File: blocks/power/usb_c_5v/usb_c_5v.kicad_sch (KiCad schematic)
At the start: 3 parts, among them J1 USB Type-C Receptacle 16-pin 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

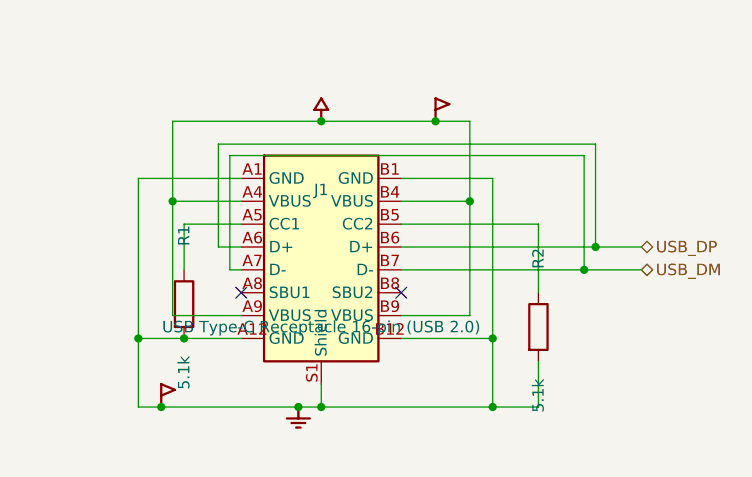
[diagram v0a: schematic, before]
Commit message: 가독 규칙 5종 기계화 + USB-C 블록 전면 재배치 + usb_c_16p 심볼 확폭 (사용자 검토 반영)
'글자 겹침 금지, 라인-심볼/라인-라인 겹침 금지, 전압 표기, 부품 식별,
값-라인 겹침 금지' — rules/schematic-readability.md R1~R6으로 성문화하고
check_block에 기계 강제:
- R2 배선 동축 중첩 / R3 심볼 몸체 통과 / R1·R6 텍스트 겹침(커널 SVG의
  mm 단위 투명 텍스트 상자 실측 — 렌더 중복 오탐 제거, 상자는 실측형)
- 게이트가 실제로 잡아낸 것: J1 참조·부품명이 핀명들과 겹침, R1 몸체 위
  배선 통과, 마주보는 핀 이름 중앙 충돌 -> 전부 수정
- usb_c_16p 심볼 확폭 (핀 ±8.89->±11.43, 몸체 ±10.16) + pin_names offset
  1.524 + Shield->SH: 좁은 몸체의 글자 밀집이 근본 원인이라 부품 차원 수리
- 블록: 전압 표기(+5V 레일 Value 표시), 부품 식별(USB-C 16P/5.1k),
  좌측 차선 재설계(GND 41.91/VBUS 44.45/CC1-R1 40.64/D+ 49.53/D- 50.8)
- 번들 심볼 갱신 + PCM 패치 (usb_c_16p 확폭 반영)
전 게이트 PASS: 하네스 ERC 0 / R1·R2·R3·R6 위반 0 / i2c_pullup 회귀 통과
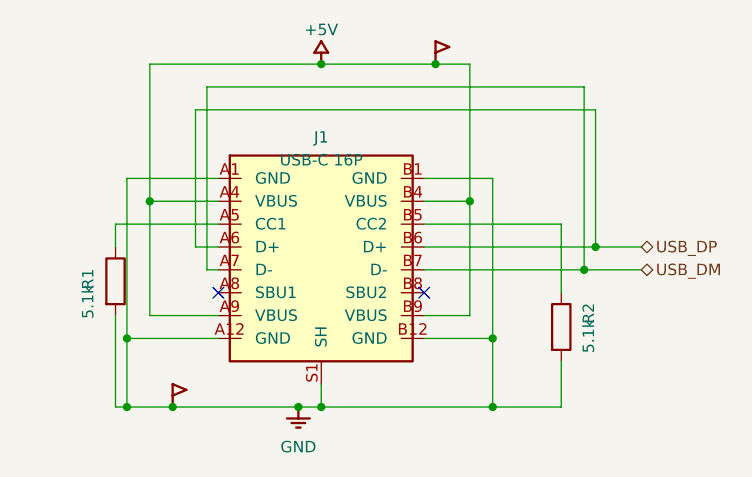
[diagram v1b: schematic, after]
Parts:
- J1: value USB Type-C Receptacle 16-pin (USB 2.0) -> USB-C 16P
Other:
- moved on the sheet: R1, R2

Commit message: 가독 규칙 R7~R10 기계화 + USB-C 블록 v3 (2차 검토 반영)
'심볼 내부 글자-외곽 겹침 / 저항이 옆 라인과 너무 가까움 / 라인 간격 균일 /
참조기호 다음 값 + 단위 표기' — rules R7~R10으로 성문화, check_block에 강제:
- R7 글자-외곽선 겹침 / R8 배선-몸체 여백 1.27 / R9 평행 배선 최소 2.54
- 게이트 적발 -> 근본 수리: usb_c_16p **핀 길이 5.08 (커넥터 관례)** —
  짧은 핀 위 번호가 외곽선을 침범하던 원인. S1도 연장(레일 직결).
- 블록 v3: 차선 전면 재설계 — 좌 5차선/우 5차선 균일 2.54 간격,
  저항을 바깥 차선으로(여백 확보), 값 표기 '5.1kΩ' (R10 단위).
- 부품은 전부 파트릴 카탈로그 참조 (없으면 파트릴에 등록 후 사용 — 확인됨)
전 게이트 PASS (ERC 0 / R1~R9 위반 0 / i2c_pullup 회귀 OK), PCM 패치
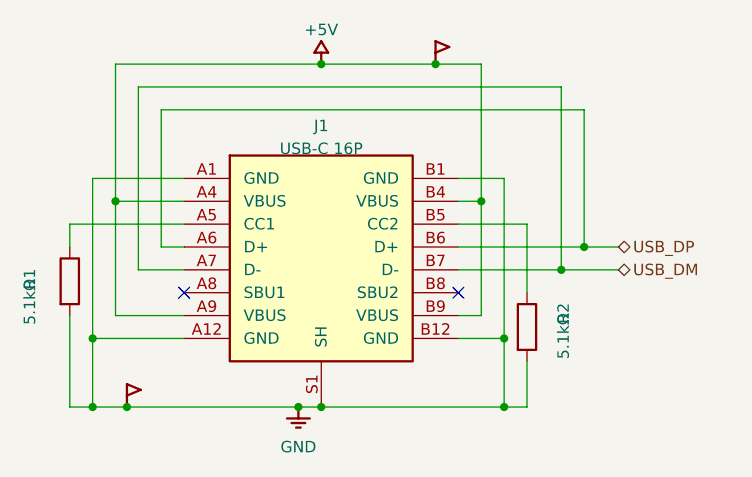
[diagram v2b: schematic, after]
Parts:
- R1, R2: value 5.1k -> 5.1kΩ
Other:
- moved on the sheet: J1, R1, R2
